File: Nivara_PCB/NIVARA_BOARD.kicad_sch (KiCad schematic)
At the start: 3 parts, among them U1 ESP32-S3-WROOM-1

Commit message: Actualización del pcb
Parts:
- renumbered C1 to C6
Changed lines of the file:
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@@
 		(on_board yes)
 		(dnp no)
-		(property "Reference" "C1"
+		(property "Reference" "C6"
 			(at 116.84 69.8499 0)
 			(effects
@@
 			(project ""
 				(path "/13184db0-a71d-4054-b13a-bbf46d2b100d/4e7fa7f2-8bf5-4f9c-874d-fa1b4fd76f92"
-					(reference "C1")
+					(reference "C6")
 					(unit 1)
 				)

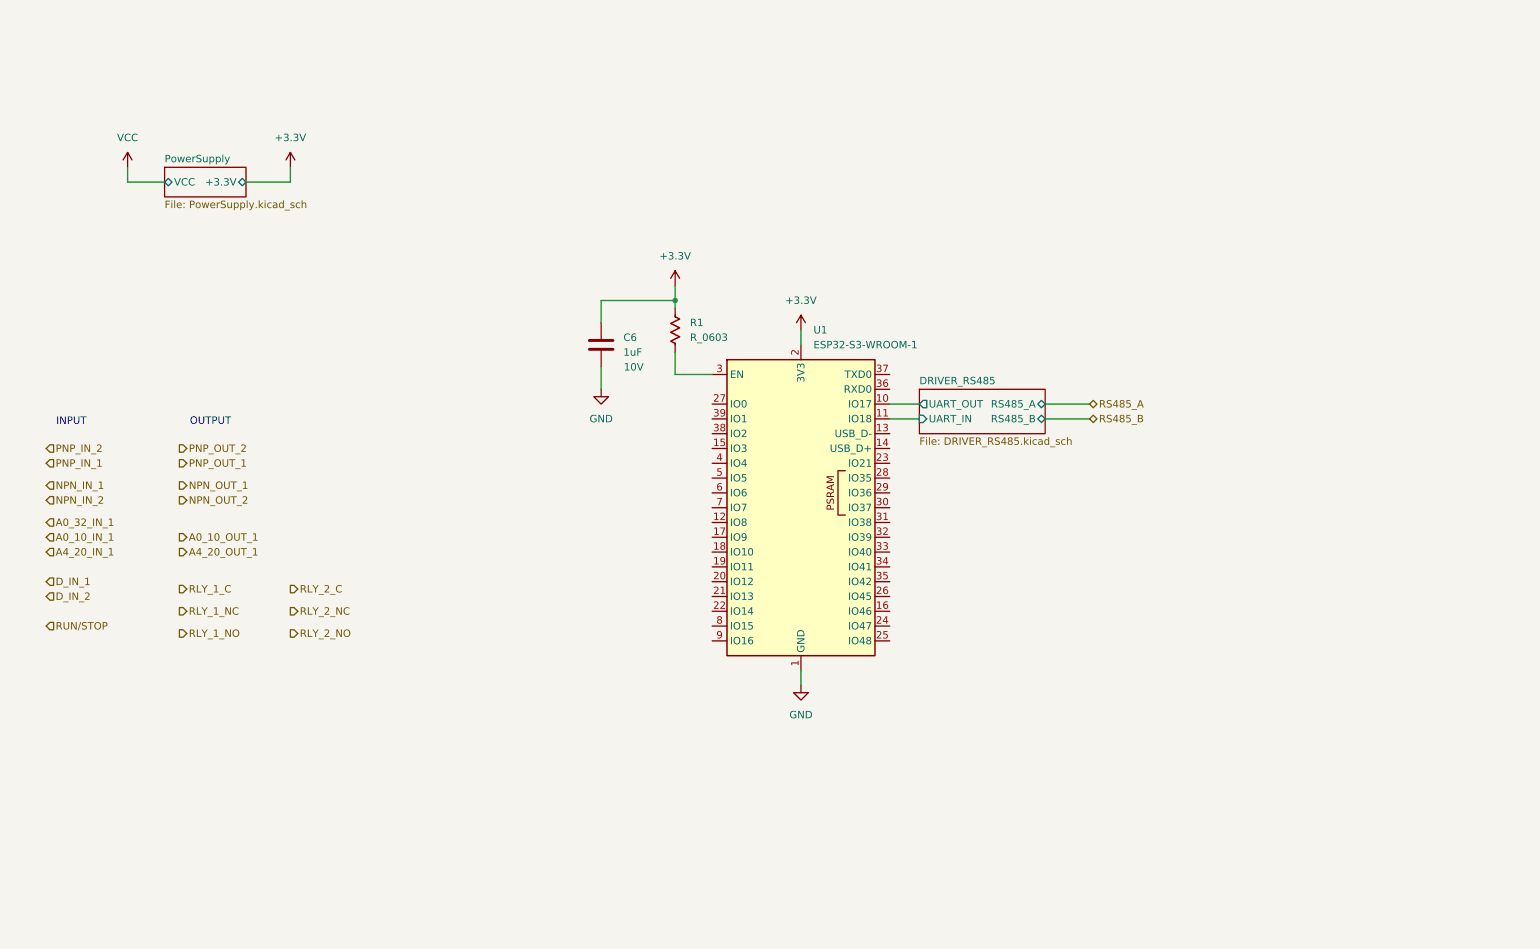
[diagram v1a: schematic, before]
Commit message: Fuente de 12V para activar optoacopladores y relés
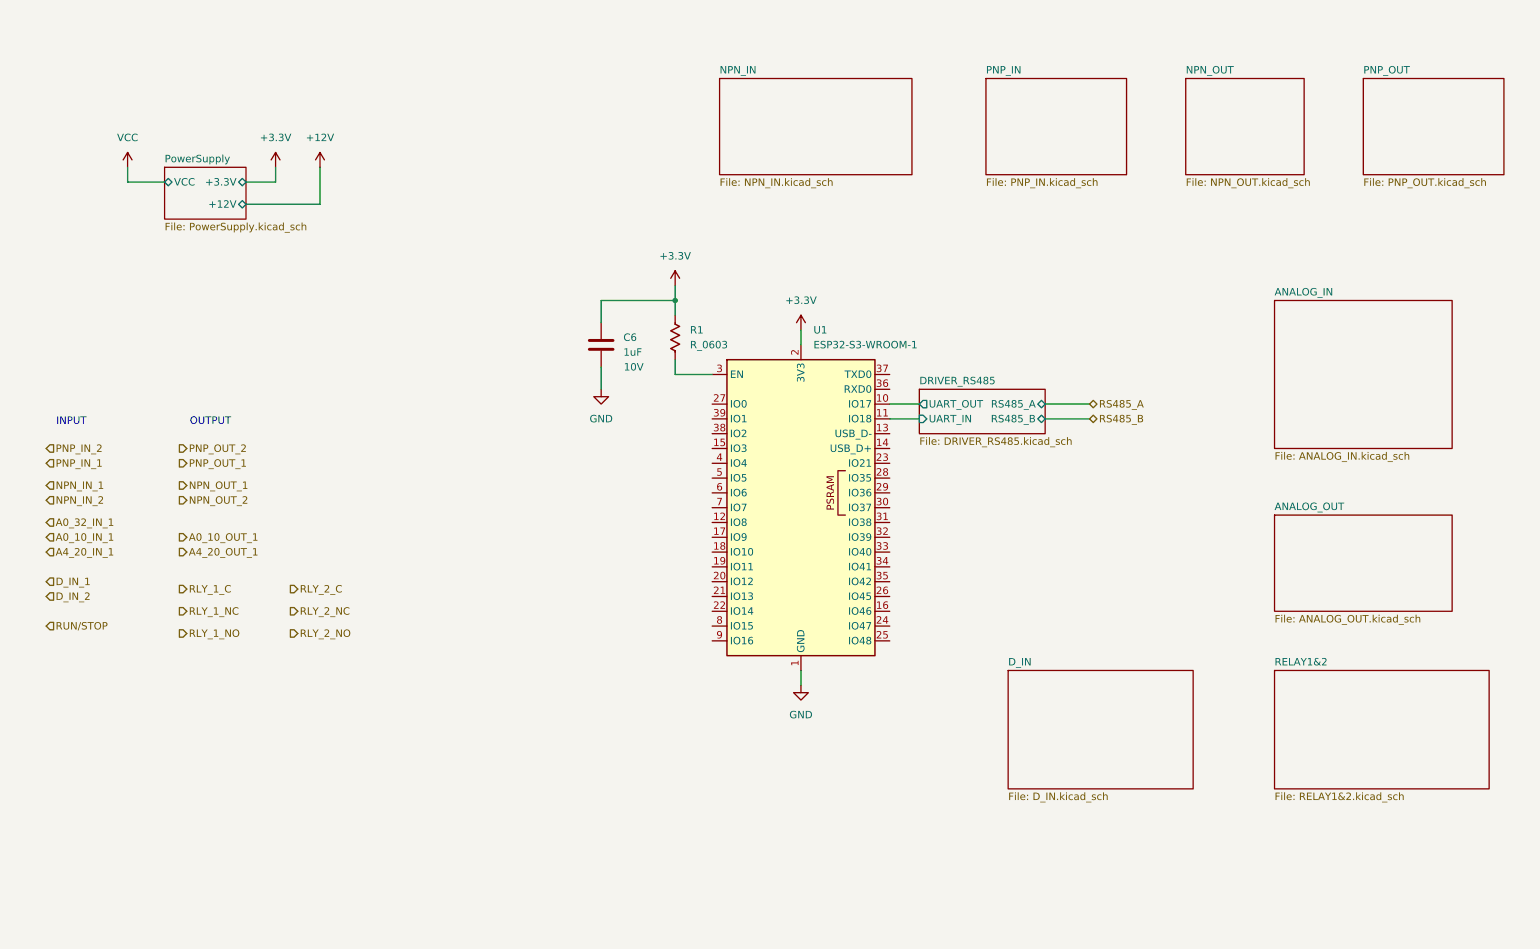
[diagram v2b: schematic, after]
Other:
- added sheet ANALOG_IN (ANALOG_IN.kicad_sch)
- added sheet ANALOG_OUT (ANALOG_OUT.kicad_sch)
- added sheet D_IN (D_IN.kicad_sch)
- added sheet NPN_IN (NPN_IN.kicad_sch)
- added sheet NPN_OUT (NPN_OUT.kicad_sch)
- added sheet PNP_IN (PNP_IN.kicad_sch)
- added sheet PNP_OUT (PNP_OUT.kicad_sch)
- added sheet RELAY1&2 (RELAY1&2.kicad_sch)
- sheet PowerSupply ports: added +12V; removed none
- moved on the sheet: R1

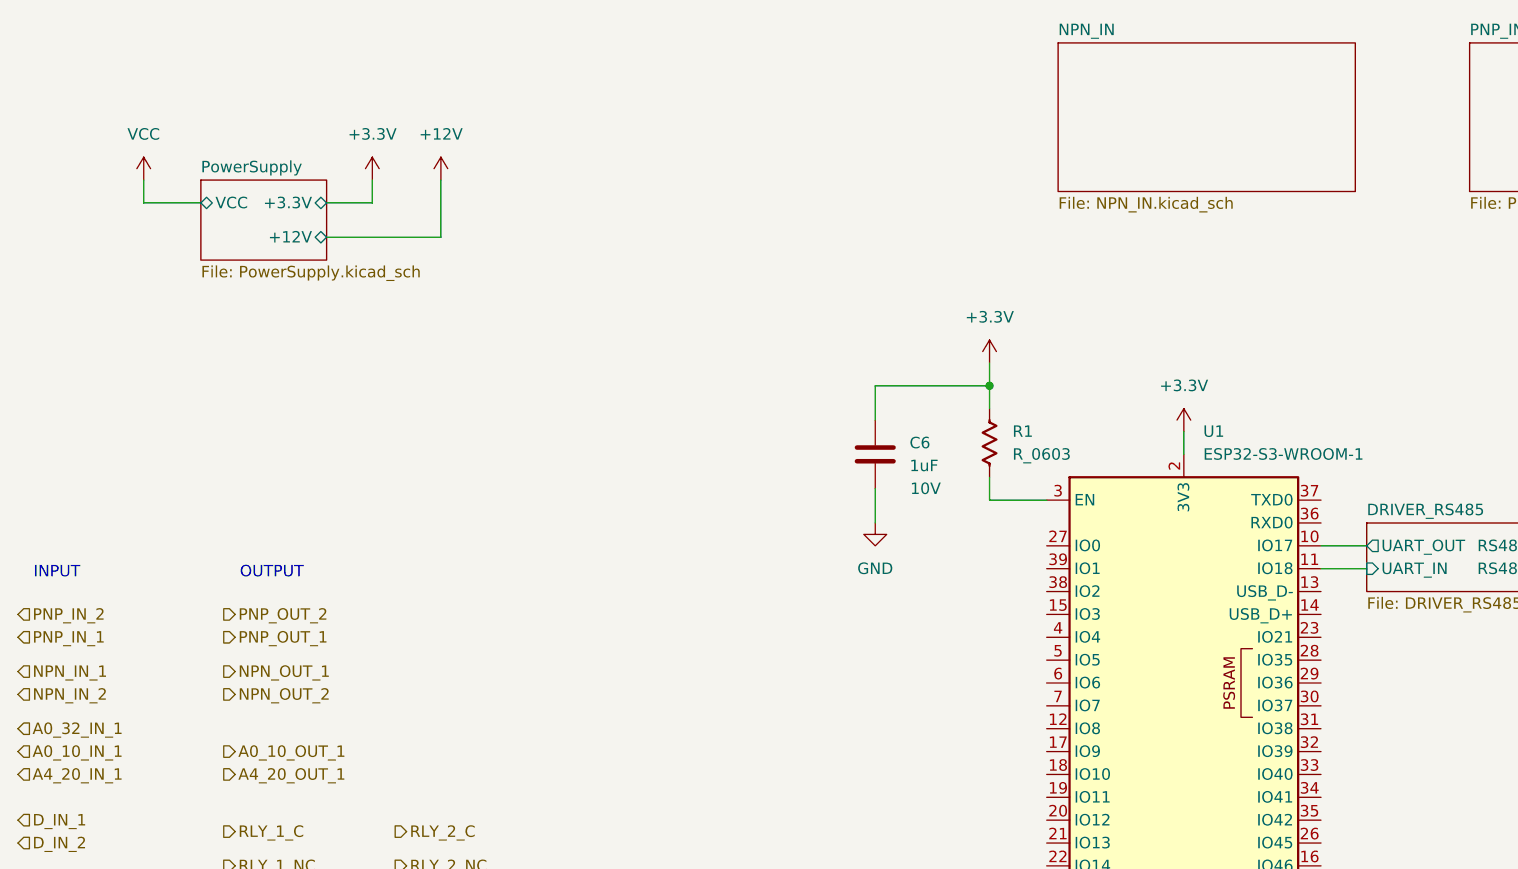
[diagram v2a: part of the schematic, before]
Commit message: Cambio a fuente de 5V para utilizar reles HF49FD Es mejor utilizar una fuente de 5V para alimentar los reles y los periféricos en general, que 12V
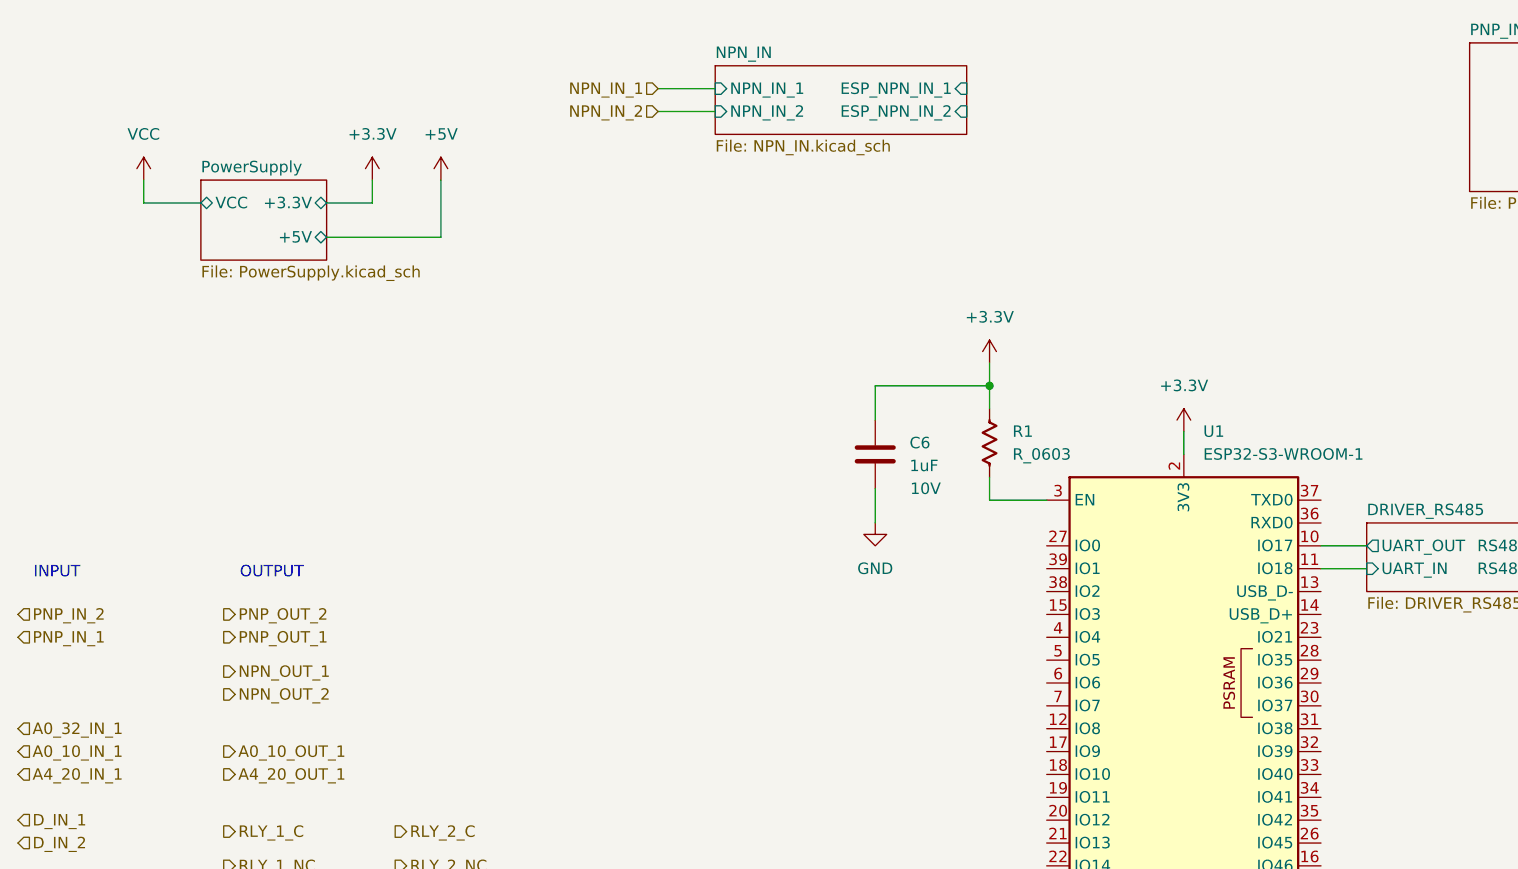
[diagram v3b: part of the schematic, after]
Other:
- sheet NPN_IN ports: added ESP_NPN_IN_1, ESP_NPN_IN_2, NPN_IN_1, NPN_IN_2; removed none
- sheet PowerSupply ports: added +5V; removed +12V
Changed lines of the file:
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@@
+	(wire
+		(pts
+			(xy 88.9 30.48) (xy 95.25 30.48)
+		)
+		(stroke
+			(width 0)
+			(type default)
+		)
+	)
 	(wire
 		(pts
@@
 	(wire
 		(pts
+			(xy 88.9 33.02) (xy 95.25 33.02)
+		)
+		(stroke
+			(width 0)
+			(type default)
+		)
+	)
+	(wire
+		(pts
 			(xy 31.75 40.64) (xy 31.75 43.18)
 		)
@@
 		)
 	)
-	(hierarchical_label "NPN_IN_2"
-		(shape input)
-		(at 17.78 97.79 0)
-		(effects
-			(font
-				(size 1.27 1.27)
-			)
-			(justify left)
-		)
-	)
 	(hierarchical_label "RUN{slash}STOP"
 		(shape input)
@@
 		)
 	)
+	(hierarchical_label "NPN_IN_2"
+		(shape input)
+		(at 88.9 33.02 180)
+		(effects
+			(font
+				(size 1.27 1.27)
+			)
+			(justify right)
+		)
+	)
 	(hierarchical_label "RLY_2_C"
 		(shape output)
@@
 		)
 	)
+	(hierarchical_label "NPN_IN_1"
+		(shape input)
+		(at 88.9 30.48 180)
+		(effects
+			(font
+				(size 1.27 1.27)
+			)
+			(justify right)
+		)
+	)
 	(hierarchical_label "PNP_OUT_1"
 		(shape output)
@@
 		(shape input)
 		(at 17.78 91.44 0)
-		(effects
-			(font
-				(size 1.27 1.27)
-			)
-			(justify left)
-		)
-	)
-	(hierarchical_label "NPN_IN_1"
-		(shape input)
-		(at 17.78 95.25 0)
 		(effects
 			(font
@@
 			)
 		)
-		(property "Value" "+12V"
+		(property "Value" "+5V"
 			(at 64.77 35.56 0)
 			(effects
@@
 	)
 	(sheet
-		(at 133.35 25.4)
-		(size 33.02 16.51)
+		(at 95.25 27.94)
+		(size 27.94 7.62)
 		(exclude_from_sim no)
 		(in_bom yes)
@@
 		)
 		(property "Sheetname" "NPN_IN"
-			(at 133.35 24.6884 0)
+			(at 95.25 27.2284 0)
 			(effects
 				(font
@@
 		)
 		(property "Sheetfile" "NPN_IN.kicad_sch"
-			(at 133.35 42.4946 0)
+			(at 95.25 36.1446 0)
 			(effects
 				(font
@@
 				)
 				(justify left top)
+			)
+		)
+		(pin "ESP_NPN_IN_1" input
+			(at 123.19 30.48 0)
+			(effects
+				(font
+					(size 1.27 1.27)
+				)
+				(justify right)
+			)
+		)
+		(pin "ESP_NPN_IN_2" input
+			(at 123.19 33.02 0)
+			(effects
+				(font
+					(size 1.27 1.27)
+				)
+				(justify right)
+			)
+		)
+		(pin "NPN_IN_1" input
+			(at 95.25 30.48 180)
+			(effects
+				(font
+					(size 1.27 1.27)
+				)
+				(justify left)
+			)
+		)
+		(pin "NPN_IN_2" input
+			(at 95.25 33.02 180)
+			(effects
+				(font
+					(size 1.27 1.27)
+				)
+				(justify left)
 			)
 		)
@@
 			)
 		)
-		(pin "+12V" bidirectional
+		(pin "+5V" bidirectional
 			(at 52.07 46.99 0)
 			(effects

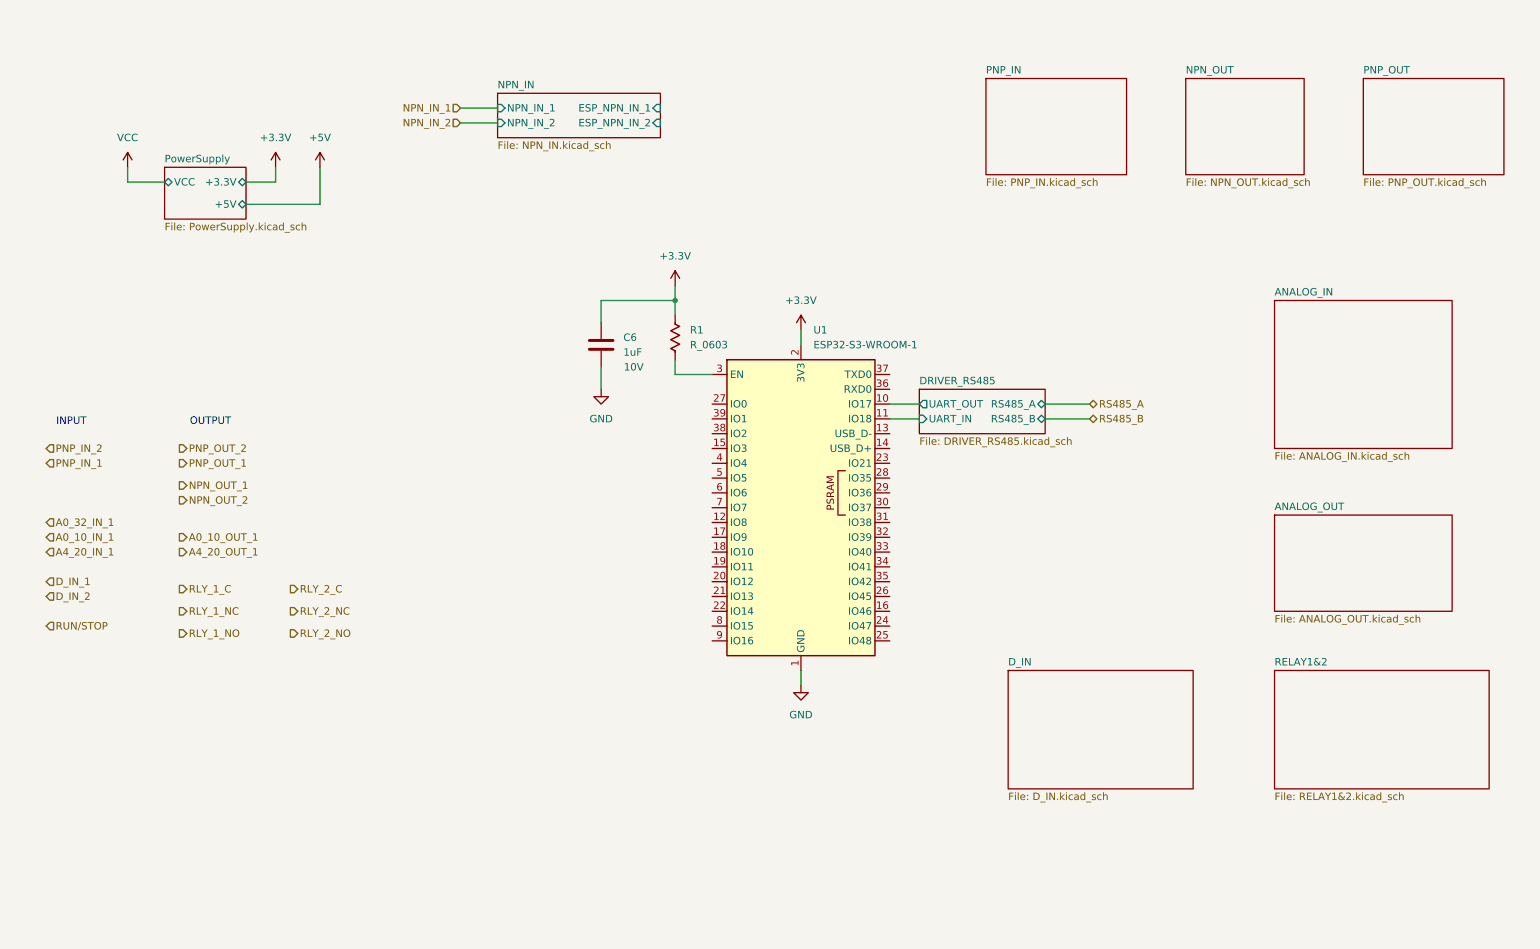
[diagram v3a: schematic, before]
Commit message: Añadido de funciones NPN/PNP
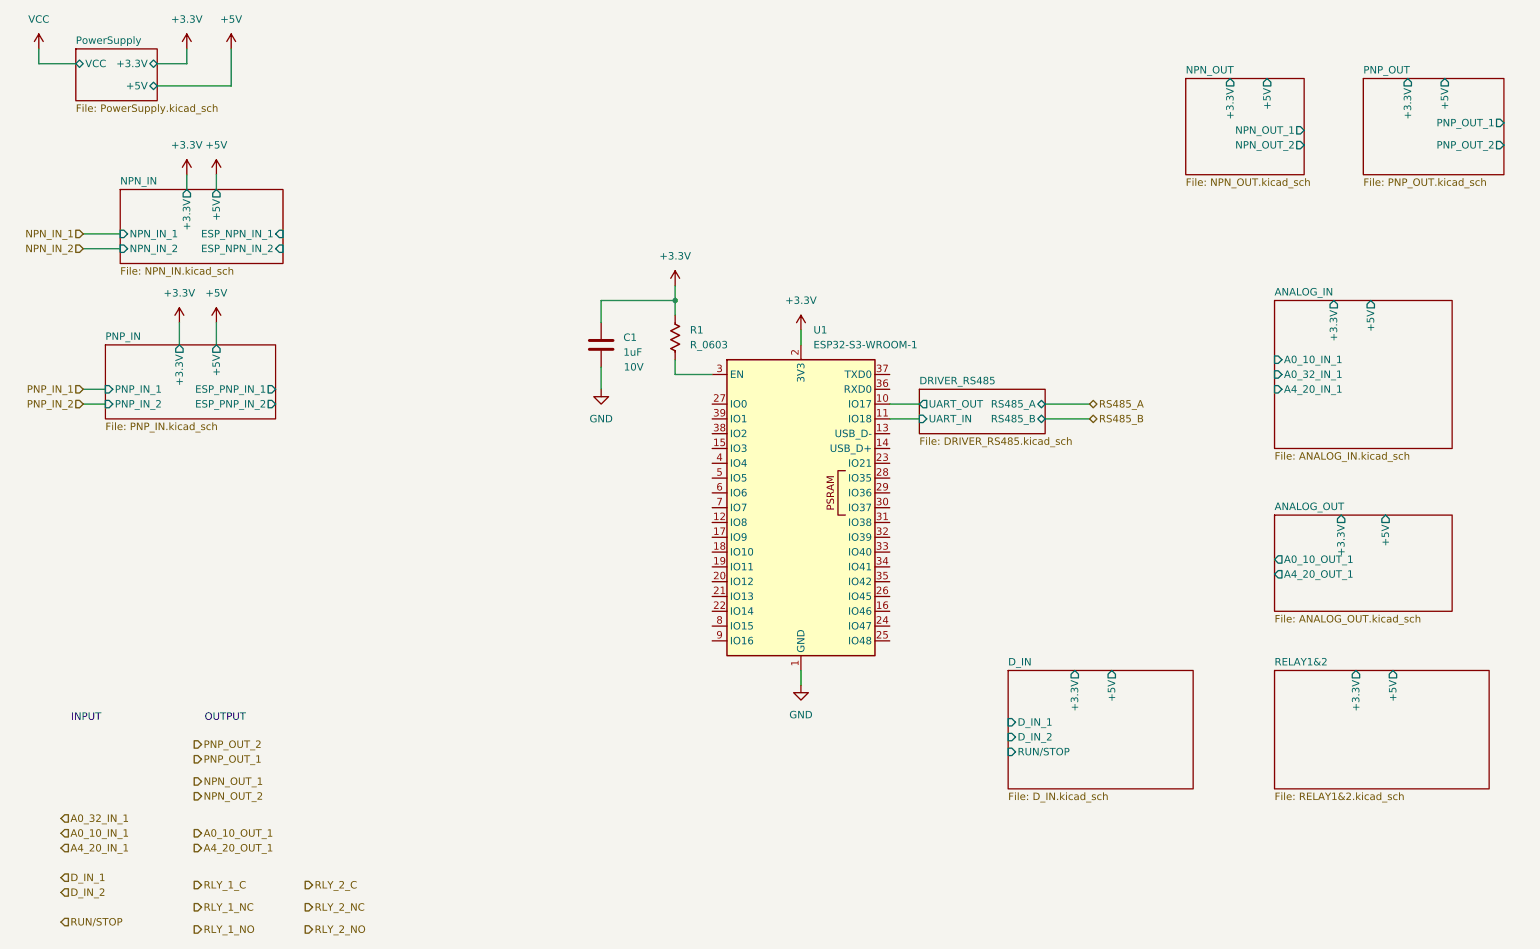
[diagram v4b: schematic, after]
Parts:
- renumbered C6 to C1
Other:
- sheet ANALOG_IN ports: added +3.3V, +5V, A0_10_IN_1, A0_32_IN_1, A4_20_IN_1; removed none
- sheet ANALOG_OUT ports: added +3.3V, +5V, A0_10_OUT_1, A4_20_OUT_1; removed none
- sheet D_IN ports: added +3.3V, +5V, D_IN_1, D_IN_2, RUN/STOP; removed none
- sheet NPN_IN ports: added +3.3V, +5V; removed none
- sheet NPN_OUT ports: added +3.3V, +5V, NPN_OUT_1, NPN_OUT_2; removed none
- sheet PNP_IN ports: added +3.3V, +5V, ESP_PNP_IN_1, ESP_PNP_IN_2, PNP_IN_1, PNP_IN_2; removed none
- sheet PNP_OUT ports: added +3.3V, +5V, PNP_OUT_1, PNP_OUT_2; removed none
- sheet RELAY1&2 ports: added +3.3V, +5V; removed none
